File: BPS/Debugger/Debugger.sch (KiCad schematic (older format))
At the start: 28 parts, among them J1 Conn_01x03, SW1 Switch:SW_Push, U1 STM32F413RHTx, U2 NCP1117-3.3_SOT223, Y1 Crystal

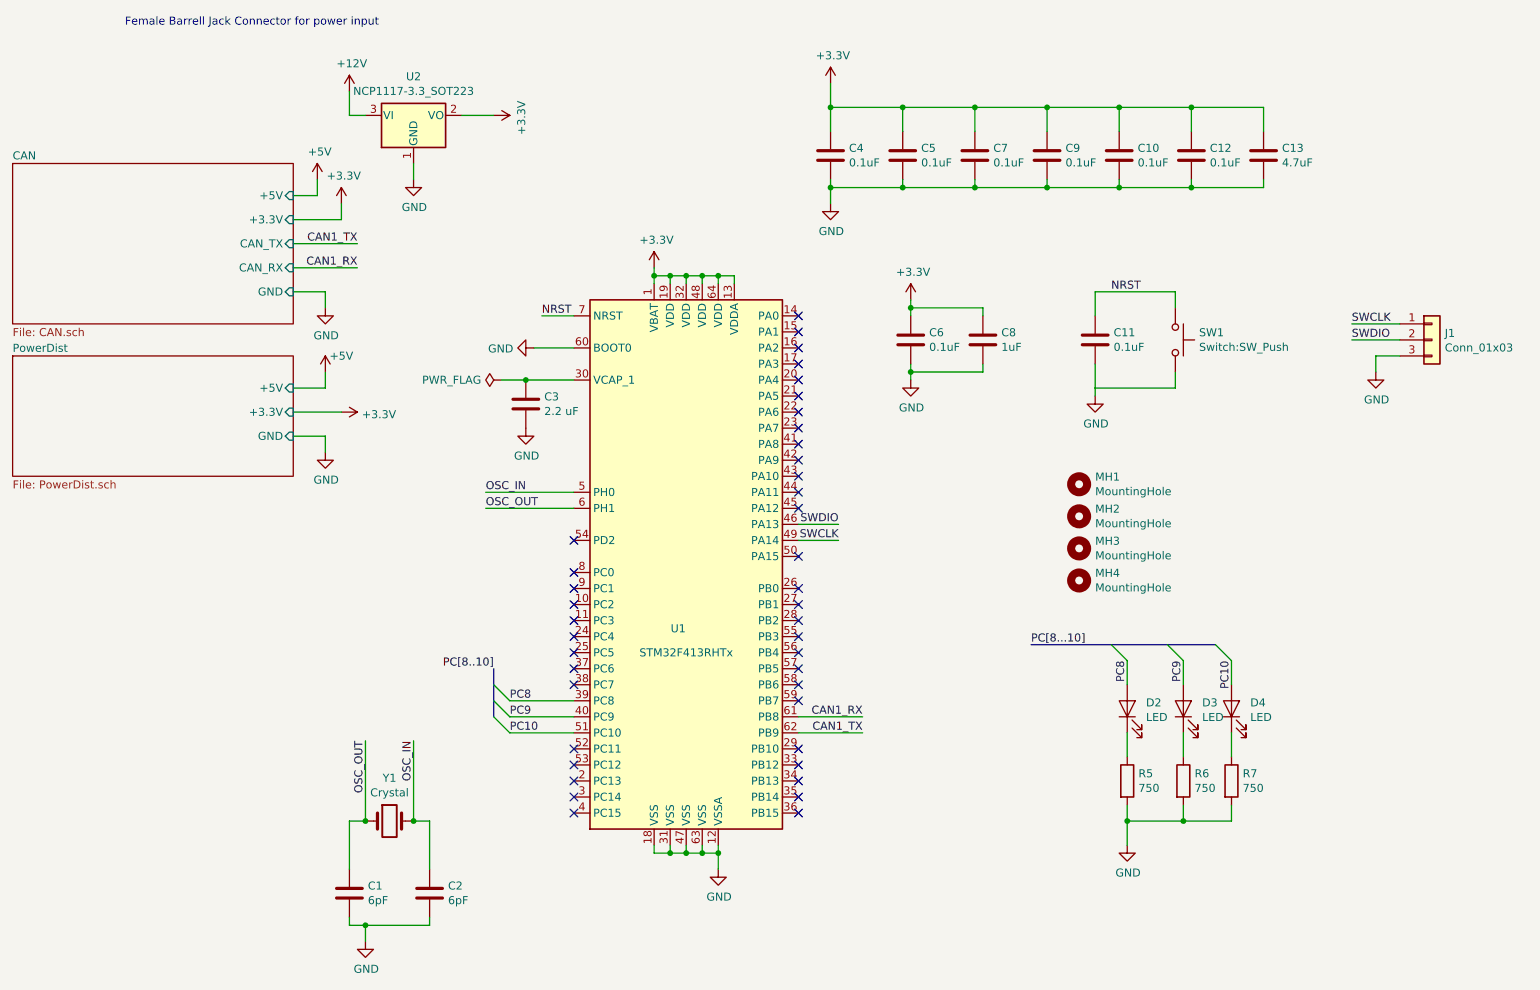
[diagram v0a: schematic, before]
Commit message: Finished debugger layout. Still needs annotations.
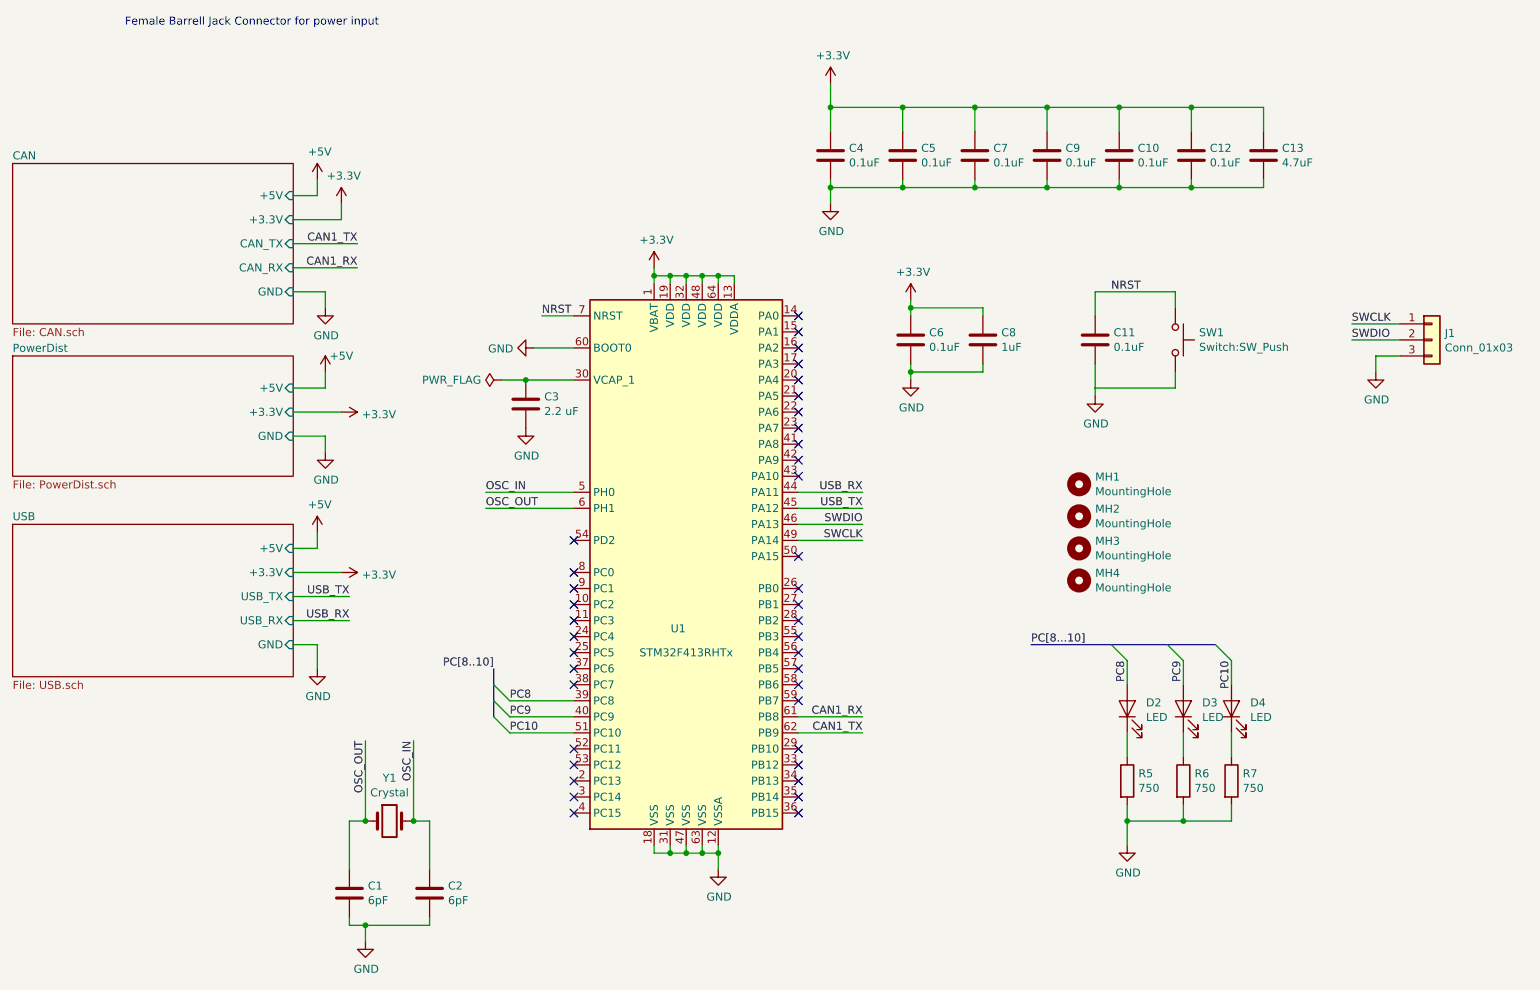
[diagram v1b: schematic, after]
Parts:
- removed U2: NCP1117-3.3_SOT223, Package_TO_SOT_SMD:SOT-223-3_TabPin2, symbol Debugger-rescue:NCP1117-3.3_SOT223-BPSMaster-cache
- J1: footprint Connector_PinHeader_2.54mm:PinHeader_1x02_P2.54mm_Vertical -> Connector_PinHeader_2.54mm:PinHeader_1x03_P2.54mm_Vertical
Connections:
- net USB_RX: now reaches U1.44 (PA11)
- net USB_TX: now reaches U1.45 (PA12)
- no-connect marks 41 -> 39
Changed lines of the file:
@@
 $Descr A4 11693 8268
 encoding utf-8
-Sheet 1 3
+Sheet 1 4
 Title ""
 Date ""
@@
 Wire Wire Line
 	7800 3050 7800 3100
-Text Label 6200 3900 2    50   ~ 0
+Text Label 6350 3900 2    50   ~ 0
 SWDIO
-Text Label 6200 4000 2    50   ~ 0
+Text Label 6350 4000 2    50   ~ 0
 SWCLK
-Wire Wire Line
-	5950 3900 6200 3900
-Wire Wire Line
-	6200 4000 5950 4000
 $Comp
 L Mechanical:MountingHole MH1
@@
 F 0 "J1" H 9980 2792 50  0000 L CNN
 F 1 "Conn_01x03" H 9980 2701 50  0000 L CNN
-F 2 "Connector_PinHeader_2.54mm:PinHeader_1x02_P2.54mm_Vertical" H 9900 2750 50  0001 C CNN
+F 2 "Connector_PinHeader_2.54mm:PinHeader_1x03_P2.54mm_Vertical" H 9900 2750 50  0001 C CNN
 F 3 "~" H 9900 2750 50  0001 C CNN
 	1    9900 2750
@@
 Wire Wire Line
 	4000 3800 4550 3800
-$Comp
-L power:GND #PWR016
-U 1 1 5C62A6C5
-P 3550 1750
-F 0 "#PWR016" H 3550 1500 50  0001 C CNN
-F 1 "GND" H 3555 1577 50  0000 C CNN
-F 2 "" H 3550 1750 50  0001 C CNN
-F 3 "" H 3550 1750 50  0001 C CNN
-	1    3550 1750
-	1    0    0    -1
-$EndComp
-$Comp
-L power:+12V #PWR015
-U 1 1 5C62A736
-P 3150 1200
-F 0 "#PWR015" H 3150 1050 50  0001 C CNN
-F 1 "+12V" H 3165 1373 50  0000 C CNN
-F 2 "" H 3150 1200 50  0001 C CNN
-F 3 "" H 3150 1200 50  0001 C CNN
-	1    3150 1200
-	1    0    0    -1
-$EndComp
-Wire Wire Line
-	3150 1200 3150 1350
-Wire Wire Line
-	3150 1350 3250 1350
-Wire Wire Line
-	3550 1650 3550 1750
 Wire Wire Line
 	6150 1750 6150 1800
@@
 Wire Wire Line
 	6150 1800 6150 1900
-$Comp
-L Debugger-rescue:NCP1117-3.3_SOT223-BPSMaster-cache U2
-U 1 1 5C65BF96
-P 3550 1350
-F 0 "U2" H 3550 1592 50  0000 C CNN
-F 1 "NCP1117-3.3_SOT223" H 3550 1501 50  0000 C CNN
-F 2 "Package_TO_SOT_SMD:SOT-223-3_TabPin2" H 3550 1550 50  0001 C CNN
-F 3 "" H 3650 1100 50  0001 C CNN
-	1    3550 1350
-	1    0    0    -1
-$EndComp
 Text Notes 1750 800  0    50   ~ 0
 Female Barrell Jack Connector for power input
@@
 Text Label 3200 2300 2    50   ~ 0
 CAN1_RX
-$Comp
-L Debugger-rescue:+3.3V-BPSMaster-cache #PWR020
-U 1 1 5C68CA74
-P 4050 1350
-F 0 "#PWR020" H 4050 1200 50  0001 C CNN
-F 1 "+3.3V" H 4065 1523 50  0000 C CNN
-F 2 "" H 4050 1350 50  0001 C CNN
-F 3 "" H 4050 1350 50  0001 C CNN
-	1    4050 1350
-	0    1    1    0
-$EndComp
-Wire Wire Line
-	3850 1350 4050 1350
 Wire Wire Line
 	4000 3700 4550 3700
@@
 NoConn ~ 5950 3500
 NoConn ~ 5950 3600
-NoConn ~ 5950 3700
-NoConn ~ 5950 3800
 NoConn ~ 5950 4100
 NoConn ~ 5950 4300
@@
 Text Label 7400 4650 0    50   ~ 0
 PC[8...10]
+$Sheet
+S 1050 3900 1750 950
+U 5C72CE9B
+F0 "USB" 50
+F1 "USB.sch" 50
+F2 "USB_TX" I R 2800 4350 50
+F3 "USB_RX" I R 2800 4500 50
+F4 "+5V" I R 2800 4050 50
+F5 "GND" I R 2800 4650 50
+F6 "+3.3V" I R 2800 4200 50
+$EndSheet
+$Comp
+L power:+5V #PWR0112
+U 1 1 5C72CFD6
+P 2950 3950
+F 0 "#PWR0112" H 2950 3800 50  0001 C CNN
+F 1 "+5V" H 2965 4123 50  0000 C CNN
+F 2 "" H 2950 3950 50  0001 C CNN
+F 3 "" H 2950 3950 50  0001 C CNN
+	1    2950 3950
+	1    0    0    -1
+$EndComp
+Wire Wire Line
+	2800 4050 2950 4050
+Wire Wire Line
+	2950 4050 2950 3950
+$Comp
+L power:GND #PWR0113
+U 1 1 5C731088
+P 2950 4800
+F 0 "#PWR0113" H 2950 4550 50  0001 C CNN
+F 1 "GND" H 2955 4627 50  0000 C CNN
+F 2 "" H 2950 4800 50  0001 C CNN
+F 3 "" H 2950 4800 50  0001 C CNN
+	1    2950 4800
+	1    0    0    -1
+$EndComp
+Wire Wire Line
+	2800 4650 2950 4650
+Wire Wire Line
+	2950 4650 2950 4800
+Text Label 6350 3800 2    50   ~ 0
+USB_TX
+Text Label 6350 3700 2    50   ~ 0
+USB_RX
+Wire Wire Line
+	5950 4000 6350 4000
+Wire Wire Line
+	5950 3900 6350 3900
+Wire Wire Line
+	5950 3800 6350 3800
+Wire Wire Line
+	5950 3700 6350 3700
+Wire Wire Line
+	2800 4350 3150 4350
+Wire Wire Line
+	2800 4500 3150 4500
+Text Label 3150 4500 2    50   ~ 0
+USB_RX
+Text Label 3150 4350 2    50   ~ 0
+USB_TX
+Wire Wire Line
+	2800 4200 3100 4200
+$Comp
+L power:+3.3V #PWR0114
+U 1 1 5C77A083
+P 3100 4200
+F 0 "#PWR0114" H 3100 4050 50  0001 C CNN
+F 1 "+3.3V" V 3115 4328 50  0000 L CNN
+F 2 "" H 3100 4200 50  0001 C CNN
+F 3 "" H 3100 4200 50  0001 C CNN
+	1    3100 4200
+	0    1    1    0
+$EndComp
 Wire Bus Line
 	4050 4800 4050 5100
